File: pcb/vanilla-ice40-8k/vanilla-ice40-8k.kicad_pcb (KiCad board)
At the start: 6 copper layers, 50 x 50 mm, 129 parts, among them J10 Conn_01x05_Pin, J11 QSH-060-01-L-D-A, J12 QSH-060-01-L-D-A, J6 Conn_01x02_Pin, J7 Conn_01x02_Pin, J8 Conn_01x02_Pin, J9 Conn_01x06_Pin, Q1 DMG2305UX-13, U1 ICE40HX8K-CT256, U2 W25X40CLSN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

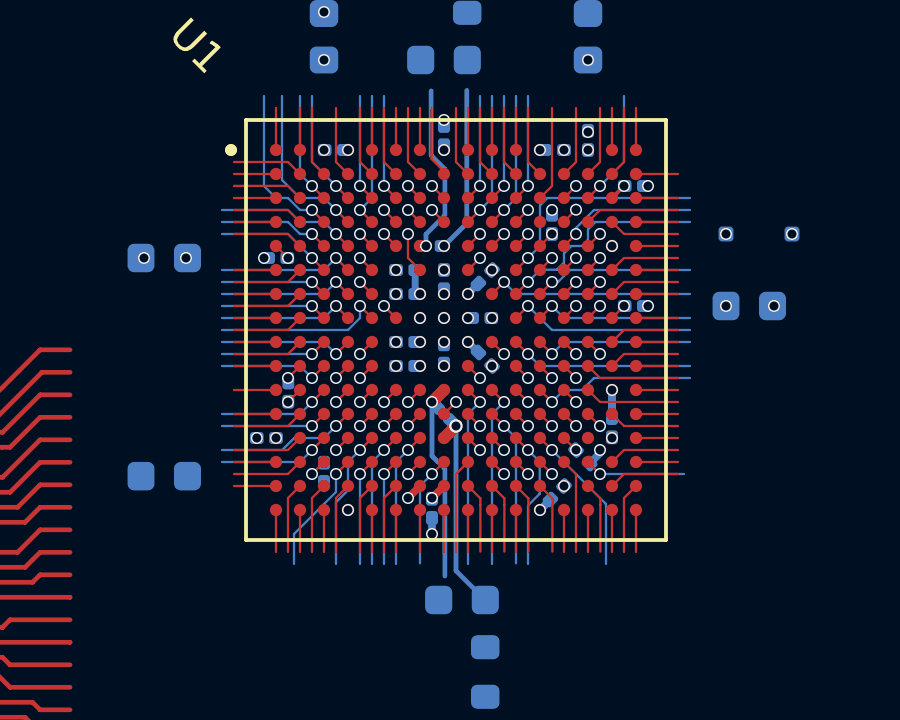
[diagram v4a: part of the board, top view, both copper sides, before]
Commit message: [pcb][hx8k] bga gnd fills
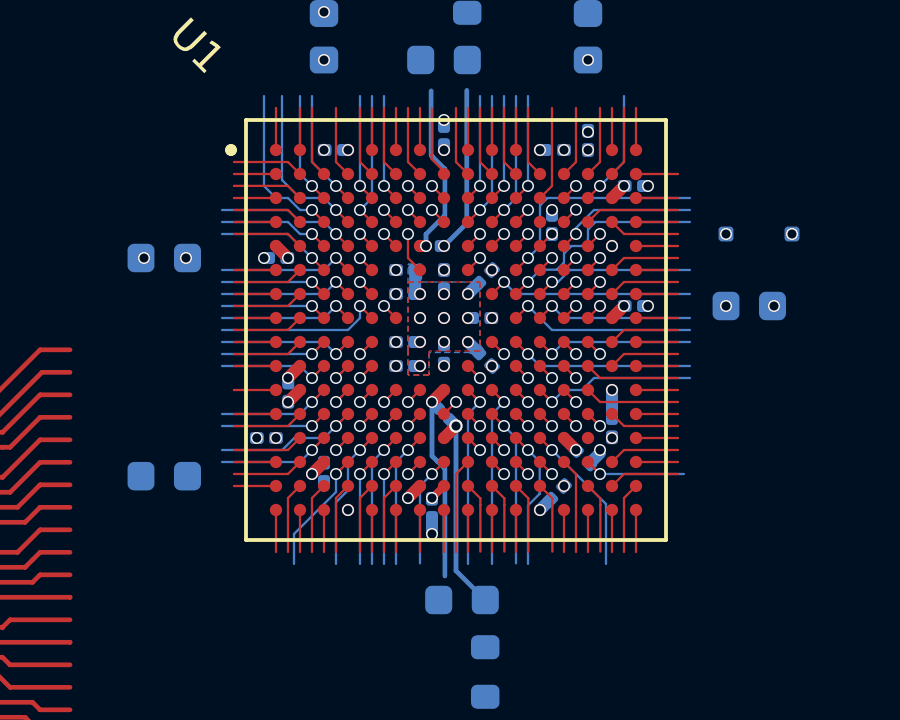
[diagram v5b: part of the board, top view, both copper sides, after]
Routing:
- added copper zone on B.Cu, net GND
- added copper zone on F.Cu, net GND
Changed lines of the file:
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@@
 		(start 112.064554 117.559951)
 		(end 112.464551 117.159951)
-		(width 0.0762)
+		(width 0.4)
 		(layer "F.Cu")
 		(net 1)
@@
 		(start 121.264554 118.759952)
 		(end 121.664554 119.159952)
-		(width 0.0762)
+		(width 0.4)
 		(layer "F.Cu")
 		(net 2)
@@
 		(start 123.264554 110.359952)
 		(end 122.864554 110.759952)
-		(width 0.127)
+		(width 0.4)
 		(layer "F.Cu")
 		(net 2)
@@
 		(start 122.864554 114.759952)
 		(end 123.264554 114.359952)
-		(width 0.0762)
+		(width 0.4)
 		(layer "F.Cu")
 		(net 2)
 	)
 	(segment
-		(start 111.664551 112.359951)
-		(end 112.064552 112.759952)
-		(width 0.0762)
+		(start 112.064552 112.759952)
+		(end 111.664554 112.359952)
+		(width 0.4)
 		(layer "F.Cu")
 		(net 2)
@@
 		(start 113.264554 119.559952)
 		(end 112.864554 119.959952)
-		(width 0.0762)
+		(width 0.4)
 		(layer "F.Cu")
 		(net 2)
@@
 		(start 112.064552 116.759952)
 		(end 112.464553 116.359952)
-		(width 0.0762)
+		(width 0.4)
 		(layer "F.Cu")
 		(net 20)
@@
 		(start 116.464554 120.359952)
 		(end 116.064554 120.759952)
-		(width 0.254)
+		(width 0.4)
 		(layer "F.Cu")
 		(net 20)
@@
 		(start 122.864555 118.094953)
 		(end 122.864554 117.159952)
-		(width 0.254)
+		(width 0.4)
 		(layer "B.Cu")
 		(net 20)
@@
 		(start 118.412003 113.6125)
 		(end 118.064553 113.95995)
-		(width 0.2286)
+		(width 0.4)
 		(layer "B.Cu")
 		(net 20)
@@
 		(start 118.412003 115.907399)
 		(end 118.064555 115.559951)
-		(width 0.2286)
+		(width 0.4)
 		(layer "B.Cu")
 		(net 20)
@@
 		(start 116.304554 113.319952)
 		(end 116.304554 113.799952)
-		(width 0.2286)
+		(width 0.4)
 		(layer "B.Cu")
 		(net 20)
@@
 		(start 120.464554 121.159951)
 		(end 120.812006 120.812499)
-		(width 0.254)
+		(width 0.4)
 		(layer "B.Cu")
 		(net 20)
@@
 		(start 116.864554 121.959952)
 		(end 116.864554 121.424952)
-		(width 0.254)
+		(width 0.4)
 		(layer "B.Cu")
 		(net 20)
@@
 		(start 122.464554 119.265048)
 		(end 122.117102 119.6125)
-		(width 0.254)
+		(width 0.4)
 		(layer "B.Cu")
 		(net 20)
@@
 	)
 	(zone
+		(net 20)
+		(net_name "GND")
+		(layer "F.Cu")
+		(hatch edge 0.5)
+		(priority 6)
+		(connect_pads yes
+			(clearance 0)
+		)
+		(min_thickness 0.25)
+		(filled_areas_thickness no)
+		(fill yes
+			(thermal_gap 1)
+			(thermal_bridge_width 1)
+		)
+		(polygon
+			(pts
+				(xy 116.064554 113.559952) (xy 118.464554 113.559952) (xy 118.464554 115.859952) (xy 116.764554 115.859952)
+				(xy 116.764554 116.659952) (xy 116.064554 116.659952) (xy 116.064554 115.859952)
+			)
+		)
+	)
+	(zone
 		(net 1)
 		(net_name "+1V2")
@@
 		(min_thickness 0.25)
 		(filled_areas_thickness no)
-		(fill
+		(fill yes
 			(thermal_gap 0.5)
 			(thermal_bridge_width 0.5)
@@
 		(min_thickness 0.25)
 		(filled_areas_thickness no)
-		(fill
+		(fill yes
 			(thermal_gap 0.5)
 			(thermal_bridge_width 0.5)
@@
 		(min_thickness 0.0254)
 		(filled_areas_thickness no)
-		(fill
+		(fill yes
 			(thermal_gap 0.5)
 			(thermal_bridge_width 0.5)
@@
 		(min_thickness 0.25)
 		(filled_areas_thickness no)
-		(fill
+		(fill yes
 			(thermal_gap 0.5)
 			(thermal_bridge_width 0.5)
@@
 		(min_thickness 0.25)
 		(filled_areas_thickness no)
-		(fill
+		(fill yes
 			(thermal_gap 0.5)
 			(thermal_bridge_width 0.5)
@@
 		(min_thickness 0.0254)
 		(filled_areas_thickness no)
-		(fill
+		(fill yes
 			(thermal_gap 0.5)
 			(thermal_bridge_width 0.5)
@@
 		(min_thickness 0.0254)
 		(filled_areas_thickness no)
-		(fill
+		(fill yes
 			(thermal_gap 0.5)
 			(thermal_bridge_width 0.5)
@@
 		(net 20)
 		(net_name "GND")
+		(layer "B.Cu")
+		(hatch edge 0.5)
+		(priority 6)
+		(connect_pads yes
+			(clearance 0)
+		)
+		(min_thickness 0.25)
+		(filled_areas_thickness no)
+		(fill yes
+			(thermal_gap 1)
+			(thermal_bridge_width 1)
+		)
+		(polygon
+			(pts
+				(xy 116.064554 112.959952) (xy 116.514554 112.959952) (xy 116.514554 113.559952) (xy 118.464554 113.559952)
+				(xy 118.464554 115.659952) (xy 118.664554 115.909952) (xy 118.414554 116.159952) (xy 118.114554 115.909952)
+				(xy 116.764554 115.909952) (xy 116.764554 116.659952) (xy 116.064554 116.659952) (xy 116.064554 115.859952)
+			)
+		)
+	)
+	(zone
+		(net 20)
+		(net_name "GND")
 		(layer "In1.Cu")
 		(hatch edge 0.5)
@@
 		(min_thickness 0.0254)
 		(filled_areas_thickness no)
-		(fill
+		(fill yes
 			(thermal_gap 0.5)
 			(thermal_bridge_width 0.5)
@@
 		(min_thickness 0.25)
 		(filled_areas_thickness no)
-		(fill
+		(fill yes
 			(thermal_gap 0.5)
 			(thermal_bridge_width 0.5)
@@
 		(min_thickness 0.1)
 		(filled_areas_thickness no)
-		(fill
+		(fill yes
 			(thermal_gap 0.5)
 			(thermal_bridge_width 0.5)

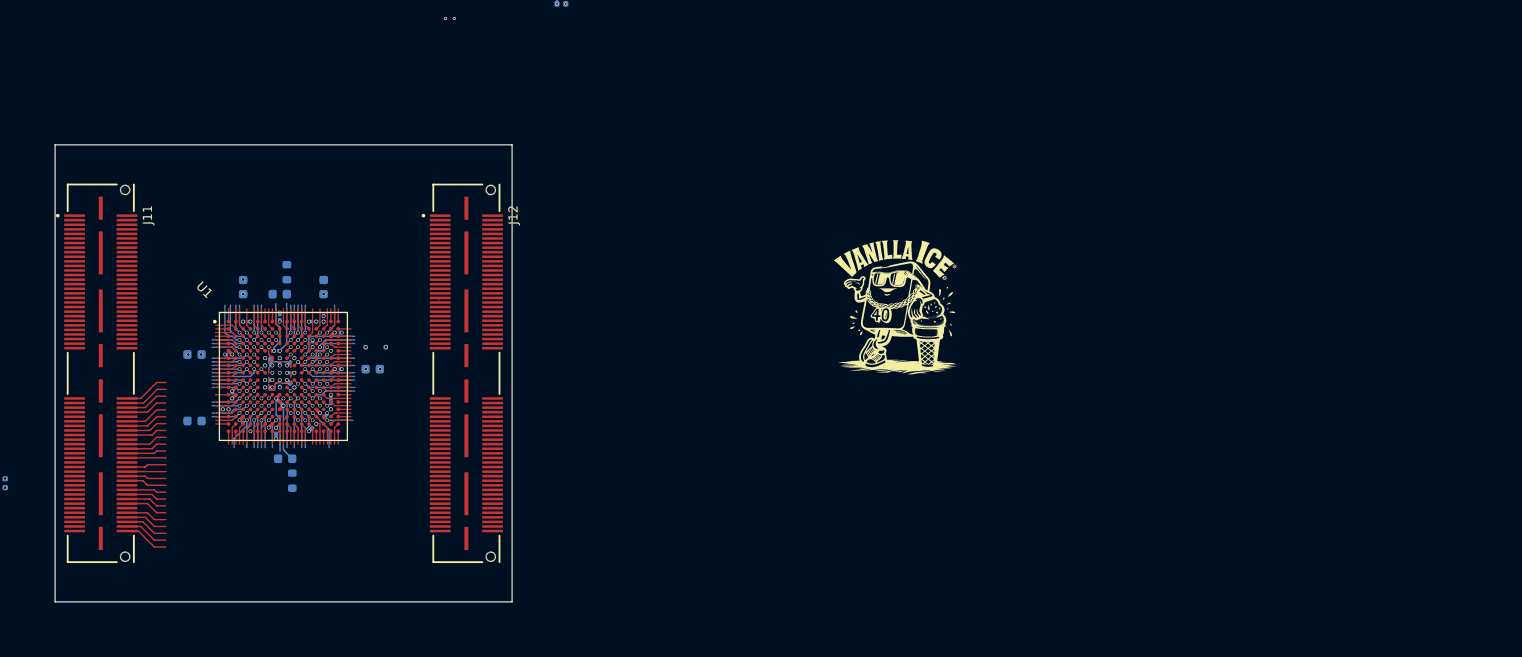
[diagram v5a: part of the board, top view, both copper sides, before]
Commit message: [pcb][hx8k] bga centered
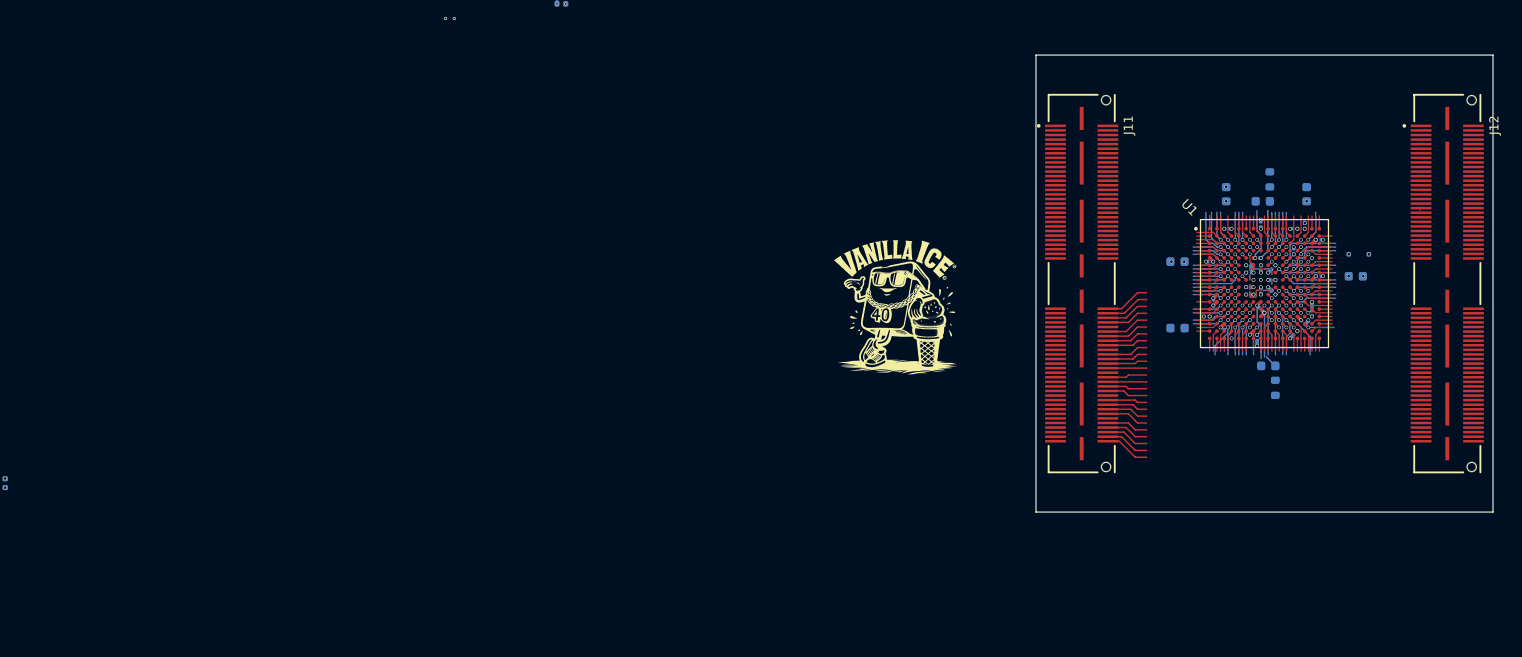
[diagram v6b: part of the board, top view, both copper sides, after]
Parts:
- moved C30 108.0 mm to (235.0, 104.2)
- moved C12 108.0 mm to (224.8, 96.0)
- moved C2 108.0 mm to (229.6, 95.2)
- moved C10 108.0 mm to (225.4, 114.0)
- moved D1 108.0 mm to (235.3, 101.8)
- moved C15 108.0 mm to (215.5, 109.9)
- moved R11 108.0 mm to (225.6, 93.6)
- moved C25 108.0 mm to (215.5, 102.6)
- moved C20 108.0 mm to (220.8, 95.2)
- moved R10 108.0 mm to (226.2, 116.4)
- moved C26 107.8 mm to (219.1, 102.6)
- moved C31 107.8 mm to (230.9, 100.2)
- moved C33 107.8 mm to (230.9, 104.2)
- moved C9 107.8 mm to (224.6, 107.8)
- moved C22 107.8 mm to (228.3, 99.0)
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
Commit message: [pcb][hx8k] moved and rotated
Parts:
- moved G*** 276.8 mm to (-86.2, 51.1)
- moved BUT1 232.9 mm to (-87.3, 142.5)
- moved C1 232.9 mm to (-145.2, 111.6)
- moved C47 232.9 mm to (-112.9, 137.6)
- moved J10 232.9 mm to (-107.3, 145.2)
- moved R12 232.9 mm to (-131.0, 139.6)
- moved R14 232.9 mm to (-133.5, 139.6)
- moved R16 232.9 mm to (-102.3, 139.6)
- moved R18 232.9 mm to (-121.0, 138.8)
- moved R21 232.9 mm to (-121.0, 141.4)
- moved R22 232.9 mm to (-110.0, 140.9)
- moved R25 232.9 mm to (-107.3, 139.5)
- moved R8 232.9 mm to (-84.4, 143.6)
- moved C46 232.9 mm to (-112.6, 138.8)
- moved J9 232.9 mm to (-136.0, 145.2)
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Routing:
- net +5V: track 59.1 -> 24.1 mm
- net +1V2: track 23.6 -> 11.9 mm
- net Net-(U6-PG): track 19.1 -> 17.2 mm
- removed copper zone on In4.Cu, net +3V3
- removed copper zone on In4.Cu, net /sram programmer/FT_VCORE
- removed copper zone on In1.Cu, net GND

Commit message: [pcb][hx8k] initial IOL header assignment
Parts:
- moved BUT1 349.3 mm to (261.5, 124.5)
- moved C47 349.3 mm to (235.9, 119.6)
- moved G*** 349.3 mm to (262.6, 33.1)
- moved J10 349.3 mm to (241.5, 127.2)
- moved R12 349.3 mm to (217.8, 121.6)
- moved R14 349.3 mm to (215.3, 121.6)
- moved R16 349.3 mm to (246.5, 121.6)
- moved R17 349.3 mm to (249.1, 121.6)
- moved R18 349.3 mm to (227.8, 120.8)
- moved R21 349.3 mm to (227.8, 123.4)
- moved R22 349.3 mm to (238.8, 122.9)
- moved R24 349.3 mm to (244.0, 121.5)
- moved R25 349.3 mm to (241.5, 121.5)
- moved R8 349.3 mm to (264.4, 125.6)
- moved C46 349.3 mm to (236.2, 120.8)
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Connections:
- J11 pad 100: /IOL_12B -> unconnected-(J11-Pad100)
- J11 pad 101: unconnected-(J11-Pad101) -> /IOL_18A
- J11 pad 102: /IOL_15B -> /IOL_17B
- J11 pad 103: unconnected-(J11-Pad103) -> /IOL_16B
- J11 pad 104: /IOL_15A -> /IOL_18B
- J11 pad 105: unconnected-(J11-Pad105) -> /IOL_19B
- J11 pad 106: /IOL_16A -> /IOL_20B
- J11 pad 107: unconnected-(J11-Pad107) -> /IOL_17A
- J11 pad 108: /IOL_17B -> /IOL_21B
- J11 pad 110: /IOL_18B -> unconnected-(J11-Pad110)
- J11 pad 111: unconnected-(J11-Pad111) -> /IOL_22B
- J11 pad 112: /IOL_20B -> /IOL_24A
- J11 pad 113: unconnected-(J11-Pad113) -> /IOL_21A
- J11 pad 114: /IOL_21B -> /IOL_25A
- J11 pad 115: unconnected-(J11-Pad115) -> /IOL_24B
- J11 pad 116: /IOL_24A -> /IOL_26A
- J11 pad 117: unconnected-(J11-Pad117) -> /IOL_26B
- J11 pad 118: /IOL_25A -> /IOL_25B
- J11 pad 119: unconnected-(J11-Pad119) -> /IOL_23B
- J11 pad 120: /IOL_26A -> /IOL_22A
- J11 pad 61: unconnected-(J11-Pad61) -> /IOL_1A
- J11 pad 62: unconnected-(J11-Pad62) -> /IOL_1B
- J11 pad 63: unconnected-(J11-Pad63) -> /IOL_6B
- J11 pad 64: unconnected-(J11-Pad64) -> /IOL_2B
- J11 pad 65: unconnected-(J11-Pad65) -> /IOL_8B
- J11 pad 66: unconnected-(J11-Pad66) -> /IOL_3B
- J11 pad 67: unconnected-(J11-Pad67) -> /IOL_2A
- J11 pad 68: unconnected-(J11-Pad68) -> /IOL_3A
- J11 pad 71: unconnected-(J11-Pad71) -> /IOL_4A
- J11 pad 72: unconnected-(J11-Pad72) -> /IOL_4B
- J11 pad 73: unconnected-(J11-Pad73) -> /IOL_5A
- J11 pad 74: unconnected-(J11-Pad74) -> /IOL_5B
- J11 pad 75: unconnected-(J11-Pad75) -> /IOL_8A
- J11 pad 76: /IOT_215 -> /IOL_7B
- J11 pad 77: unconnected-(J11-Pad77) -> /IOL_6A
- J11 pad 78: /IOL_2B -> /IOL_10B
- J11 pad 80: /IOL_3B -> unconnected-(J11-Pad80)
- J11 pad 81: unconnected-(J11-Pad81) -> /IOL_10A
- J11 pad 82: /IOL_3A -> /IOL_9B
- J11 pad 83: unconnected-(J11-Pad83) -> /IOL_9A
- J11 pad 84: /IOL_4B -> /IOL_13B
- J11 pad 85: unconnected-(J11-Pad85) -> /IOL_19A
- J11 pad 86: /IOL_5B -> /IOL_11B
- J11 pad 87: unconnected-(J11-Pad87) -> /IOL_11A
- J11 pad 88: /IOL_7B -> /IOL_14B
- J11 pad 90: /IOL_9B -> unconnected-(J11-Pad90)
- J11 pad 91: unconnected-(J11-Pad91) -> /IOL_13A
- J11 pad 92: /IOL_10B -> /IOL_12B
- J11 pad 93: unconnected-(J11-Pad93) -> /IOL_7A
- J11 pad 94: /IOL_13B -> /IOL_15B
- J11 pad 95: unconnected-(J11-Pad95) -> /IOL_20A
- J11 pad 96: /IOL_11B -> /IOL_15A
- J11 pad 97: unconnected-(J11-Pad97) -> /IOL_12A
- J11 pad 98: /IOL_14B -> /IOL_16A
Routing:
- net /IOL_3B: track 2.37 -> 11.7 mm
- net /IOL_1B: track 2.37 -> 11.1 mm
- net /IOL_5B: track 5.75 -> 12.3 mm
- net /IOL_3A: track 5.96 -> 11.1 mm
- net /IOL_22A: track 7.34 -> 12.3 mm
- net unconnected-(J11-Pad62): track 4.97 -> 0.00 mm
- net /IOL_25B: track 6.30 -> 11.2 mm
- net unconnected-(J11-Pad64): track 4.87 -> 0.00 mm
- net unconnected-(J11-Pad72): track 4.77 -> 0.00 mm
- net unconnected-(J11-Pad66): track 4.77 -> 0.00 mm
- net unconnected-(J11-Pad74): track 4.66 -> 0.00 mm
- net unconnected-(J11-Pad68): track 4.66 -> 0.00 mm
- net /IOL_4B: track 7.98 -> 12.6 mm
- net /IOL_9B: track 2.37 -> 6.93 mm
- net /IOT_215: track 10.4 -> 5.80 mm
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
